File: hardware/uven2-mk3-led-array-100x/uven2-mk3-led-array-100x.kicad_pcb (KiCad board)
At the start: 2 copper layers, 146.7 x 182.8 mm, 323 parts, among them J1 TSM-150-01-S-DH, J2 TSM-150-01-S-DH, J3 TSM-104-01-L-DH

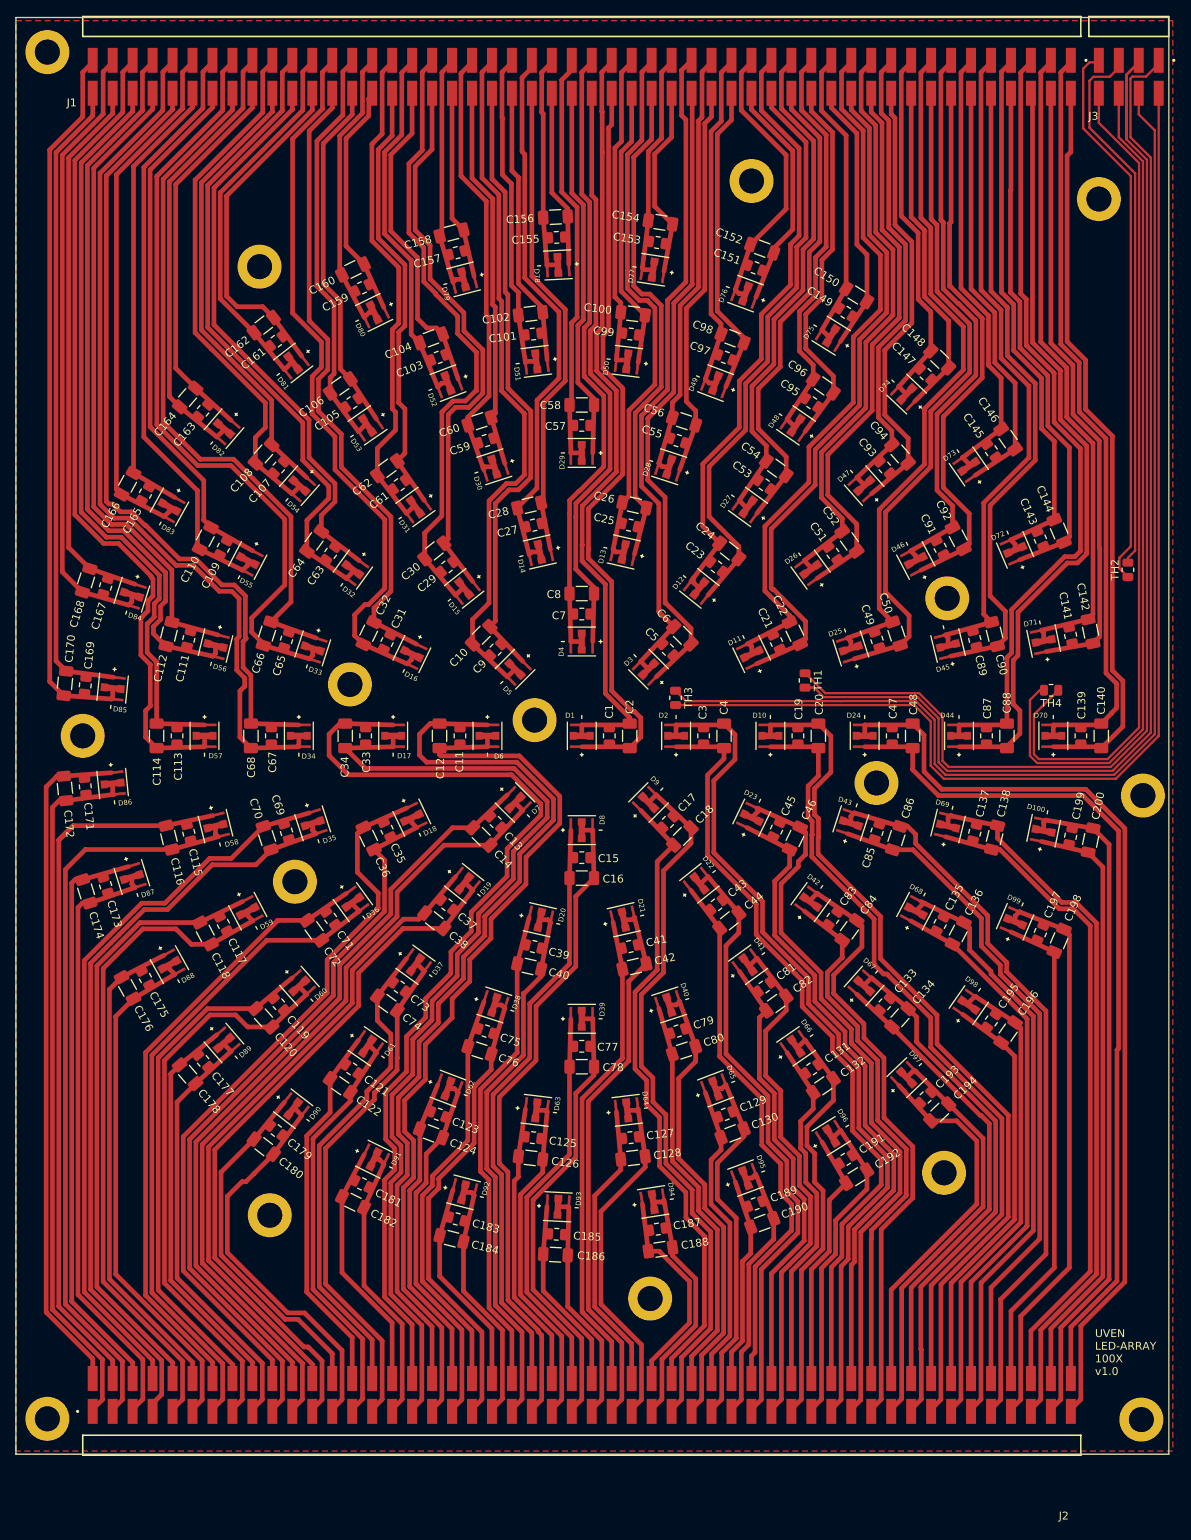
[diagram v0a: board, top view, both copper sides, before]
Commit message: added direct heat sink pad of leds
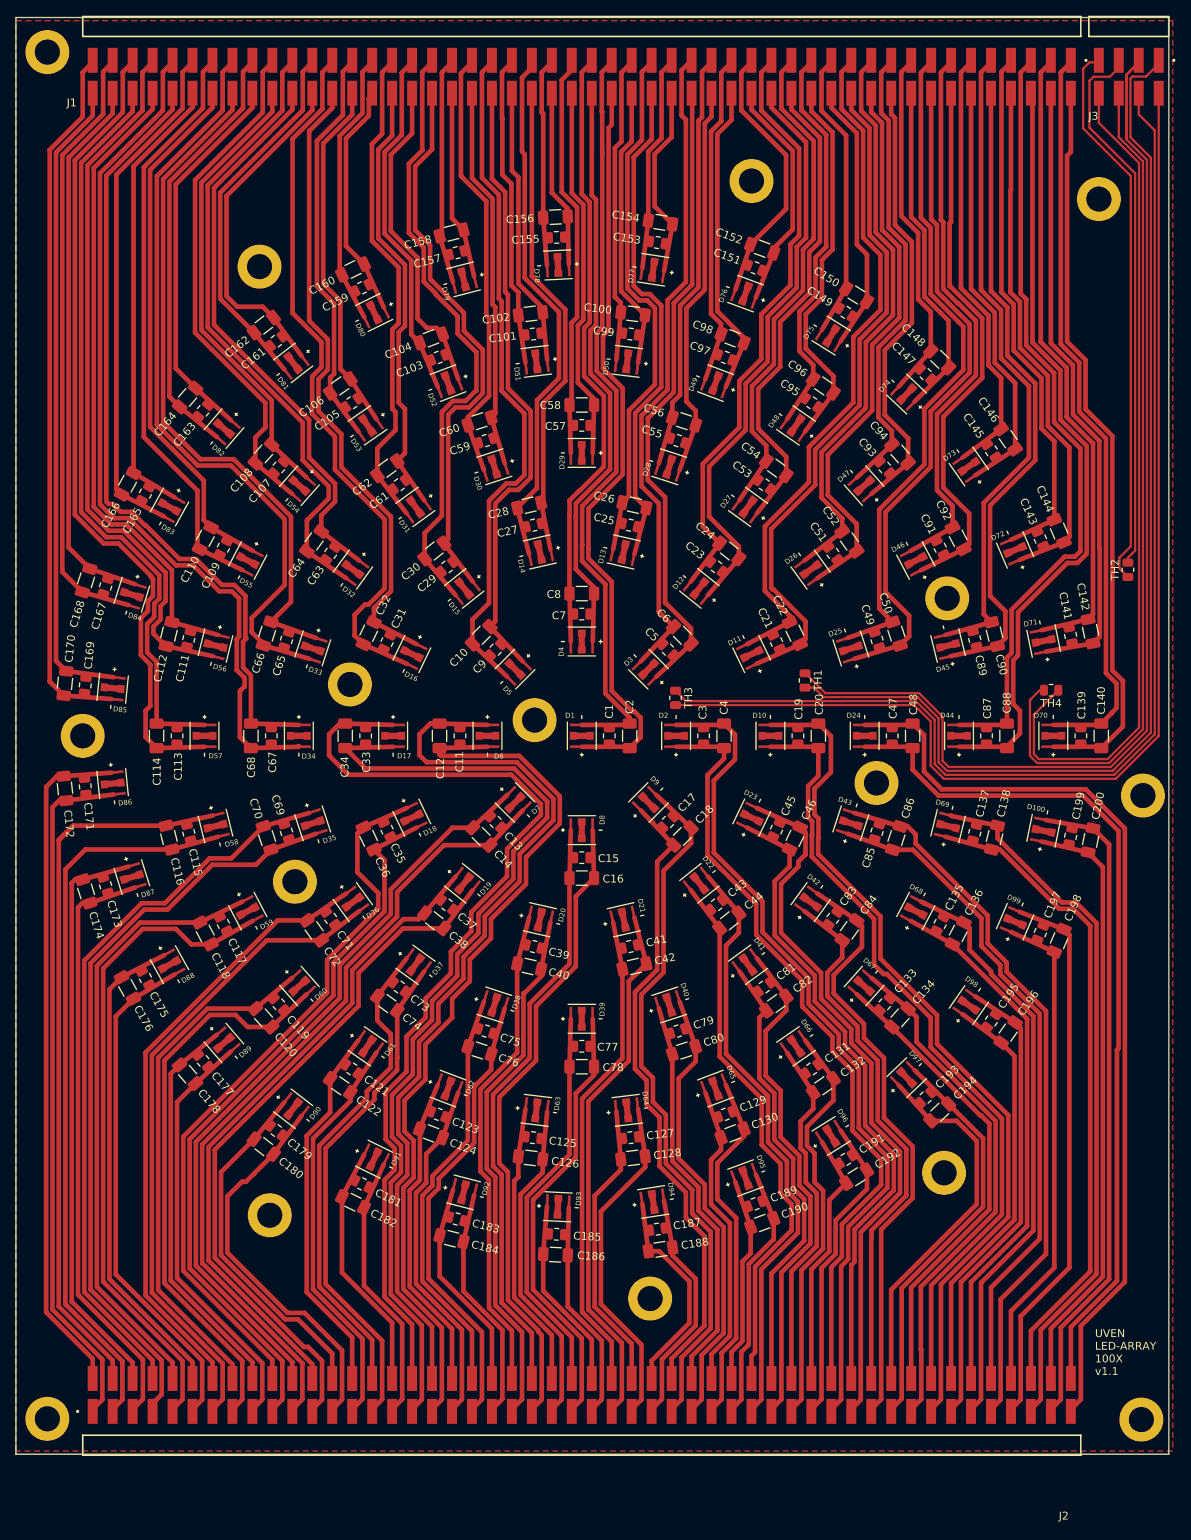
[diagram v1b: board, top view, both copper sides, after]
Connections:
- D1 pad EXP: /CATHODE_0 -> unconnected-(D1-PadEXP)
- D10 pad EXP: /CATHODE_9 -> unconnected-(D10-PadEXP)
- D100 pad EXP: /CATHODE_99 -> unconnected-(D100-PadEXP)
- D11 pad EXP: /CATHODE_10 -> unconnected-(D11-PadEXP)
- D12 pad EXP: /CATHODE_11 -> unconnected-(D12-PadEXP)
- D13 pad EXP: /CATHODE_12 -> unconnected-(D13-PadEXP)
- D14 pad EXP: /CATHODE_13 -> unconnected-(D14-PadEXP)
- D15 pad EXP: /CATHODE_14 -> unconnected-(D15-PadEXP)
- D16 pad EXP: /CATHODE_15 -> unconnected-(D16-PadEXP)
- D17 pad EXP: /CATHODE_16 -> unconnected-(D17-PadEXP)
- D18 pad EXP: /CATHODE_17 -> unconnected-(D18-PadEXP)
- D19 pad EXP: /CATHODE_18 -> unconnected-(D19-PadEXP)
- D2 pad EXP: /CATHODE_1 -> unconnected-(D2-PadEXP)
- D20 pad EXP: /CATHODE_19 -> unconnected-(D20-PadEXP)
- D21 pad EXP: /CATHODE_20 -> unconnected-(D21-PadEXP)
- D22 pad EXP: /CATHODE_21 -> unconnected-(D22-PadEXP)
- D23 pad EXP: /CATHODE_22 -> unconnected-(D23-PadEXP)
- D24 pad EXP: /CATHODE_23 -> unconnected-(D24-PadEXP)
- D25 pad EXP: /CATHODE_24 -> unconnected-(D25-PadEXP)
- D26 pad EXP: /CATHODE_25 -> unconnected-(D26-PadEXP)
- D27 pad EXP: /CATHODE_26 -> unconnected-(D27-PadEXP)
- D28 pad EXP: /CATHODE_27 -> unconnected-(D28-PadEXP)
- D29 pad EXP: /CATHODE_28 -> unconnected-(D29-PadEXP)
- D3 pad EXP: /CATHODE_2 -> unconnected-(D3-PadEXP)
- D30 pad EXP: /CATHODE_29 -> unconnected-(D30-PadEXP)
- D31 pad EXP: /CATHODE_30 -> unconnected-(D31-PadEXP)
- D32 pad EXP: /CATHODE_31 -> unconnected-(D32-PadEXP)
- D33 pad EXP: /CATHODE_32 -> unconnected-(D33-PadEXP)
- D34 pad EXP: /CATHODE_33 -> unconnected-(D34-PadEXP)
- D35 pad EXP: /CATHODE_34 -> unconnected-(D35-PadEXP)
- D36 pad EXP: /CATHODE_35 -> unconnected-(D36-PadEXP)
- D37 pad EXP: /CATHODE_36 -> unconnected-(D37-PadEXP)
- D38 pad EXP: /CATHODE_37 -> unconnected-(D38-PadEXP)
- D39 pad EXP: /CATHODE_38 -> unconnected-(D39-PadEXP)
- D4 pad EXP: /CATHODE_3 -> unconnected-(D4-PadEXP)
- D40 pad EXP: /CATHODE_39 -> unconnected-(D40-PadEXP)
- D41 pad EXP: /CATHODE_40 -> unconnected-(D41-PadEXP)
- D42 pad EXP: /CATHODE_41 -> unconnected-(D42-PadEXP)
- D43 pad EXP: /CATHODE_42 -> unconnected-(D43-PadEXP)
- D44 pad EXP: /CATHODE_43 -> unconnected-(D44-PadEXP)
- D45 pad EXP: /CATHODE_44 -> unconnected-(D45-PadEXP)
- D46 pad EXP: /CATHODE_45 -> unconnected-(D46-PadEXP)
- D47 pad EXP: /CATHODE_46 -> unconnected-(D47-PadEXP)
- D48 pad EXP: /CATHODE_47 -> unconnected-(D48-PadEXP)
- D49 pad EXP: /CATHODE_48 -> unconnected-(D49-PadEXP)
- D5 pad EXP: /CATHODE_4 -> unconnected-(D5-PadEXP)
- D50 pad EXP: /CATHODE_49 -> unconnected-(D50-PadEXP)
- D51 pad EXP: /CATHODE_50 -> unconnected-(D51-PadEXP)
- D52 pad EXP: /CATHODE_51 -> unconnected-(D52-PadEXP)
- D53 pad EXP: /CATHODE_52 -> unconnected-(D53-PadEXP)
- D54 pad EXP: /CATHODE_53 -> unconnected-(D54-PadEXP)
- D55 pad EXP: /CATHODE_54 -> unconnected-(D55-PadEXP)
- D56 pad EXP: /CATHODE_55 -> unconnected-(D56-PadEXP)
- D57 pad EXP: /CATHODE_56 -> unconnected-(D57-PadEXP)
- D58 pad EXP: /CATHODE_57 -> unconnected-(D58-PadEXP)
- D59 pad EXP: /CATHODE_58 -> unconnected-(D59-PadEXP)
- D6 pad EXP: /CATHODE_5 -> unconnected-(D6-PadEXP)
- D60 pad EXP: /CATHODE_59 -> unconnected-(D60-PadEXP)
- D61 pad EXP: /CATHODE_60 -> unconnected-(D61-PadEXP)
- D62 pad EXP: /CATHODE_61 -> unconnected-(D62-PadEXP)
- D63 pad EXP: /CATHODE_62 -> unconnected-(D63-PadEXP)
- D64 pad EXP: /CATHODE_63 -> unconnected-(D64-PadEXP)
- D65 pad EXP: /CATHODE_64 -> unconnected-(D65-PadEXP)
- D66 pad EXP: /CATHODE_65 -> unconnected-(D66-PadEXP)
- D67 pad EXP: /CATHODE_66 -> unconnected-(D67-PadEXP)
- D68 pad EXP: /CATHODE_67 -> unconnected-(D68-PadEXP)
- D69 pad EXP: /CATHODE_68 -> unconnected-(D69-PadEXP)
- D7 pad EXP: /CATHODE_6 -> unconnected-(D7-PadEXP)
- D70 pad EXP: /CATHODE_69 -> unconnected-(D70-PadEXP)
- D71 pad EXP: /CATHODE_70 -> unconnected-(D71-PadEXP)
- D72 pad EXP: /CATHODE_71 -> unconnected-(D72-PadEXP)
- D73 pad EXP: /CATHODE_72 -> unconnected-(D73-PadEXP)
- D74 pad EXP: /CATHODE_73 -> unconnected-(D74-PadEXP)
- D75 pad EXP: /CATHODE_74 -> unconnected-(D75-PadEXP)
- D76 pad EXP: /CATHODE_75 -> unconnected-(D76-PadEXP)
- D77 pad EXP: /CATHODE_76 -> unconnected-(D77-PadEXP)
- D78 pad EXP: /CATHODE_77 -> unconnected-(D78-PadEXP)
- D79 pad EXP: /CATHODE_78 -> unconnected-(D79-PadEXP)
- D8 pad EXP: /CATHODE_7 -> unconnected-(D8-PadEXP)
- D80 pad EXP: /CATHODE_79 -> unconnected-(D80-PadEXP)
- D81 pad EXP: /CATHODE_80 -> unconnected-(D81-PadEXP)
- D82 pad EXP: /CATHODE_81 -> unconnected-(D82-PadEXP)
- D83 pad EXP: /CATHODE_82 -> unconnected-(D83-PadEXP)
- D84 pad EXP: /CATHODE_83 -> unconnected-(D84-PadEXP)
- D85 pad EXP: /CATHODE_84 -> unconnected-(D85-PadEXP)
- D86 pad EXP: /CATHODE_85 -> unconnected-(D86-PadEXP)
- D87 pad EXP: /CATHODE_86 -> unconnected-(D87-PadEXP)
- D88 pad EXP: /CATHODE_87 -> unconnected-(D88-PadEXP)
- D89 pad EXP: /CATHODE_88 -> unconnected-(D89-PadEXP)
- D9 pad EXP: /CATHODE_8 -> unconnected-(D9-PadEXP)
- D90 pad EXP: /CATHODE_89 -> unconnected-(D90-PadEXP)
- D91 pad EXP: /CATHODE_90 -> unconnected-(D91-PadEXP)
- D92 pad EXP: /CATHODE_91 -> unconnected-(D92-PadEXP)
- D93 pad EXP: /CATHODE_92 -> unconnected-(D93-PadEXP)
- D94 pad EXP: /CATHODE_93 -> unconnected-(D94-PadEXP)
- D95 pad EXP: /CATHODE_94 -> unconnected-(D95-PadEXP)
- D96 pad EXP: /CATHODE_95 -> unconnected-(D96-PadEXP)
- D97 pad EXP: /CATHODE_96 -> unconnected-(D97-PadEXP)
- D98 pad EXP: /CATHODE_97 -> unconnected-(D98-PadEXP)
- D99 pad EXP: /CATHODE_98 -> unconnected-(D99-PadEXP)
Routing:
- net /CATHODE_11: track 77.4 -> 75.8 mm
- net /CATHODE_10: track 88.8 -> 87.3 mm
- net /CATHODE_96: track 53.1 -> 51.6 mm
- net /CATHODE_71: track 69.1 -> 67.6 mm
- net /CATHODE_98: track 72.0 -> 70.5 mm
- net /CATHODE_61: track 46.5 -> 45.0 mm
- net /CATHODE_51: track 46.6 -> 45.1 mm
- net /CATHODE_64: track 47.0 -> 45.5 mm
- net /CATHODE_48: track 43.8 -> 42.3 mm
- net /CATHODE_94: track 34.1 -> 32.6 mm
- net /CATHODE_75: track 35.5 -> 34.0 mm
- net /CATHODE_17: track 95.1 -> 93.6 mm
- net /CATHODE_15: track 91.9 -> 90.4 mm
- net /CATHODE_90: track 35.8 -> 34.3 mm
- net /CATHODE_79: track 36.1 -> 34.6 mm
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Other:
- board text added: "UVEN LED-ARRAY 100X v1.1"
- board text removed: "UVEN LED-ARRAY 100X v1.0"
